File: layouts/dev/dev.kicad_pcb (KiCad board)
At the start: 6 copper layers, 32.5 x 60.6 mm, 85 parts

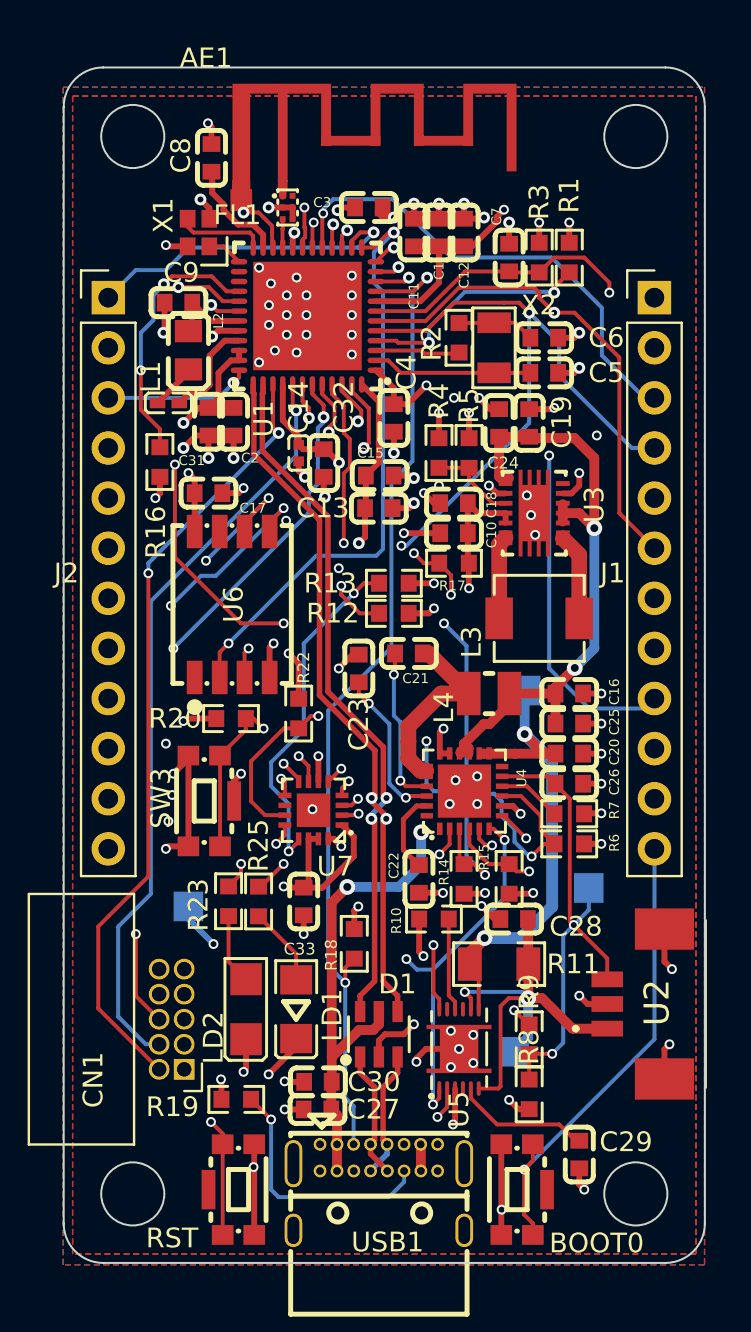
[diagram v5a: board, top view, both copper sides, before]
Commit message: fix: put the hand-tuned clearances into the script and force them on zones
Two settings changed in KiCad during layout would have been overwritten by
the next board_setup run, the same way an earlier min_clearance edit already
was. They are now in the script.

RF netclass clearance 0.30 -> 0.15. The 0.30 was a wish, not a dimension:
at the MCU the RF trace threads between pins 19-24 on a 0.5 mm pitch and
there is nowhere to move it. 0.15 is what the rest of the board uses and
still sits above JLCPCB's 0.127 minimum.

Zone clearance 0.20 -> 0.15, not the 0.10 that was asked for. Two reasons,
and the second one makes the first moot: 0.10 is below the 0.127 the README
records as JLCPCB's floor, and KiCad takes the larger of the netclass and
zone clearances anyway, so anything under CLEARANCE_MM is inert. 0.15 is
the tightest value that actually does something.

set_zones was also only applying clearance to zones it created itself, never
to the ones it found - the same gap that left every pour on
ZONE_CONNECTION_NONE. The pours were carrying their own values: 0.200 on
ground and power, and 0.100 on SYS and VBUS, which is under the fab
minimum. All six now read 0.15.

The expectation that a tighter pour would reduce fragmentation was wrong:
isolated_copper stayed at 67 either way. The setting is still right, but it
does not buy that.

Verified against the board as handed over: routing untouched at 1033
segments, zero unconnected items, zero clearance violations. Vias went 225
to 228 because the rerouting freed space under the MCU - its stitching grid
now places 22 where it placed 19, with 326 positions blocked by foreign
copper instead of 673.

Co-Authored-By: Claude Opus 5 (1M context) <noreply@anthropic.com>
Claude-Session: https://claude.ai/code/session_01BM8NndJbzBEDPtrpVjN835
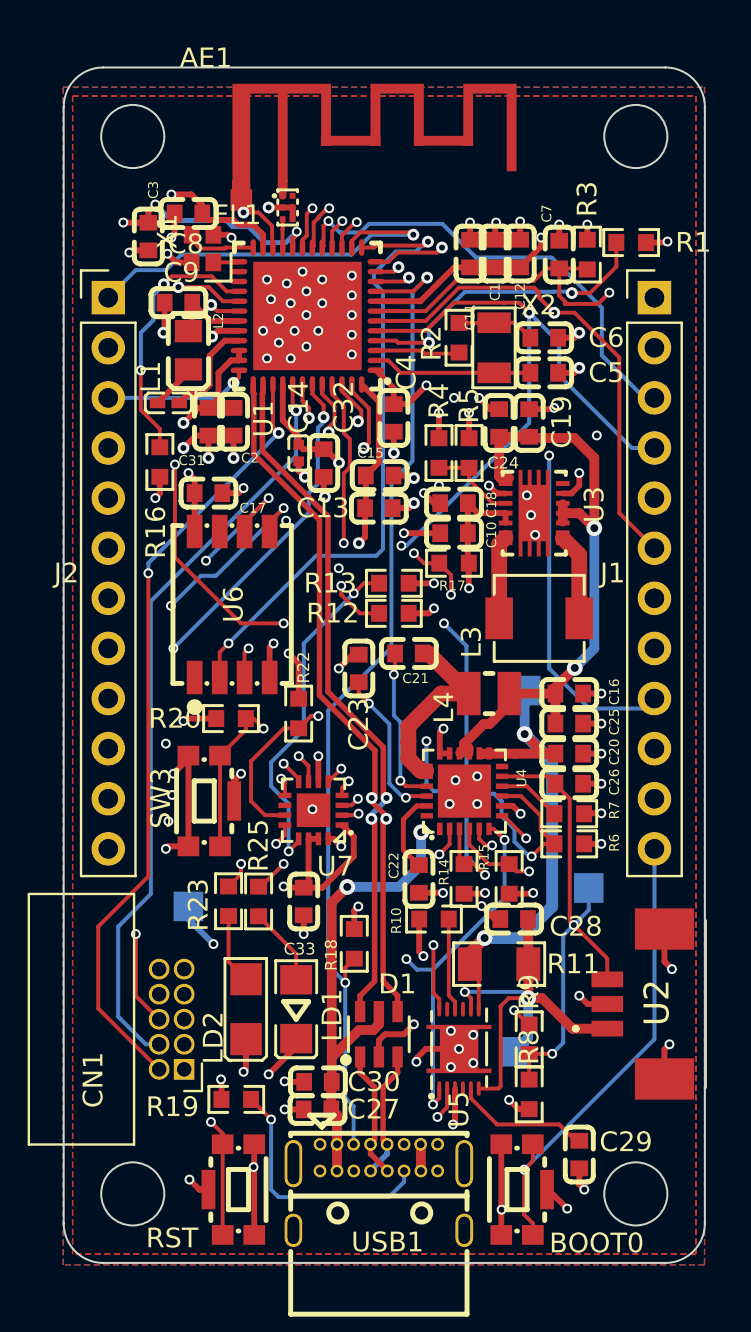
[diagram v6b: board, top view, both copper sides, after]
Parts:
- moved C3 11.3 mm to (12.7, 10.9), turned to -90 degrees
- moved R1 3.23 mm to (37.2, 11.2), turned to 0 degrees
- moved C8 3.05 mm to (14.7, 9.70), turned to 180 degrees
- moved C1 3.04 mm to (30.3, 11.7)
- moved C11 3.04 mm to (29.0, 11.7)
- moved C12 3.04 mm to (31.5, 11.7)
- moved C7 2.54 mm to (33.5, 11.8)
- moved R3 2.44 mm to (35.0, 11.8)
- moved X1 0.84 mm to (15.4, 11.5)
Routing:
- net +3V3: track 79.9 -> 89.5 mm, vias 20 -> 22
- net SD_CLK: track 42.2 -> 48.2 mm
- net REGN: track 20.0 -> 24.3 mm
- net BOOT0: track 83.7 -> 86.9 mm
- net SD_CS: track 30.3 -> 32.8 mm
- net PA9: track 15.1 -> 17.3 mm
- net NRST: track 97.8 -> 99.9 mm
- net CHG_STAT: track 53.0 -> 54.6 mm
- net SD_MISO: track 29.6 -> 31.0 mm
- net PA8: track 24.5 -> 23.5 mm
- net OSC_OUT: track 4.51 -> 3.58 mm
- net SD_MOSI: track 30.4 -> 31.2 mm
- net OSC_IN: track 1.83 -> 1.31 mm
- net GND: track 101.7 -> 101.3 mm, vias 99 -> 103

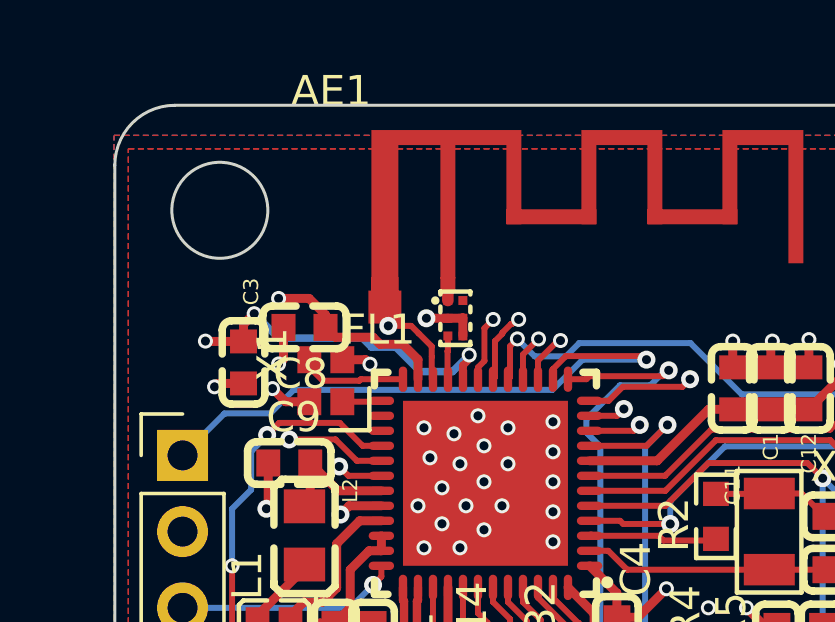
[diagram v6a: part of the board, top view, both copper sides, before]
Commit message: feat: place the antenna's shorting via from the script
The shorting via is what makes an inverted-F an antenna - the radiator is
tied to ground through the stub, and without that tie the structure is just
copper at an undefined impedance. The comment at ANTENA_KEEPOUT_MM has
assumed this via since the beginning, but it was never placed: the stub foot
from AN043 is 0.90 x 0.50 mm and a via with clearance needs 0.80 in both
axes. The landing pad added to the footprint finally gave it room.

It belongs in the script rather than in the board by hand, because
board_setup runs after every build and a via this important should be
reproducible, not remembered.

The pad is chosen geometrically, not by coordinates. It has to hold the
whole via with clearance, and it has to sit entirely below the keepout. The
second test is the one that matters: the vertical stub also passes the size
test at 0.90 mm wide, but it lies inside the keepout, and a via there would
put ground exactly where ground must not be.

Before placing, the same checks the thermal-pad stitching uses: the whole
via inside the pad copper, centre plus four points on its circumference. An
existing via within a via diameter is left alone, so repeated runs do not
pile them up - verified by running three times and finding one via at
(17.41, 9.03) each time.

Result: one 0.50/0.30 via on GND, 1.00 mm clear of the keepout, routing
untouched at 1033 segments, DRC unchanged. Every ground island on F.Cu now
has a path to the In1 plane - 55 islands, none orphaned - which also
confirms the button shields got connected during the last layout pass.

Co-Authored-By: Claude Opus 5 (1M context) <noreply@anthropic.com>
Claude-Session: https://claude.ai/code/session_01BM8NndJbzBEDPtrpVjN835
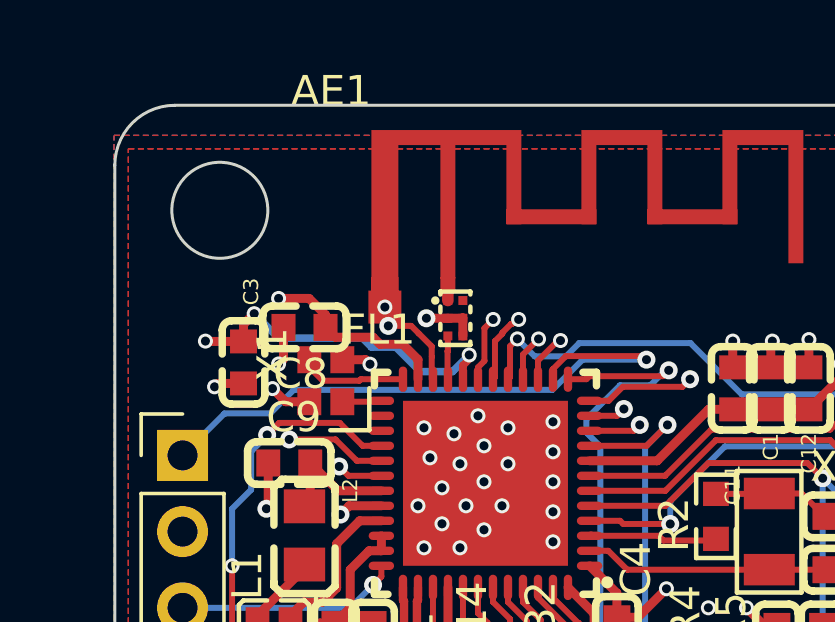
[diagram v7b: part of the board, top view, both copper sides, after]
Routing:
- net GND: vias 103 -> 104
